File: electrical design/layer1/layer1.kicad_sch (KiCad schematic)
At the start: 226 parts, among them J1 XT30-F, J10 Conn_01x02_Pin, J11 Conn_01x01_Socket, J12 Conn_01x01_Socket, J13 SH1.0 5P, J14 SH1.0 3P, J15 Conn_01x01_Socket, J2 Conn_01x01_Socket, J3 Conn_01x01_Socket, J4 XT30PW-F, J5 Conn_01x01_Socket, J6 Conn_01x01_Socket, J7 Conn_01x01_Socket, J8 Conn_01x01_Socket, J9 Conn_01x02_Pin, Q1 MOSFET-NCH-FQP30N06L, Q2 MOSFET-NCH-AO3404A, SW1 SW_SPDT, U1 CD74HC4067SM, U2 CD74HC4067SM, U3 MOUDLE-SEEEDUINO-XIAO-ESP32C3

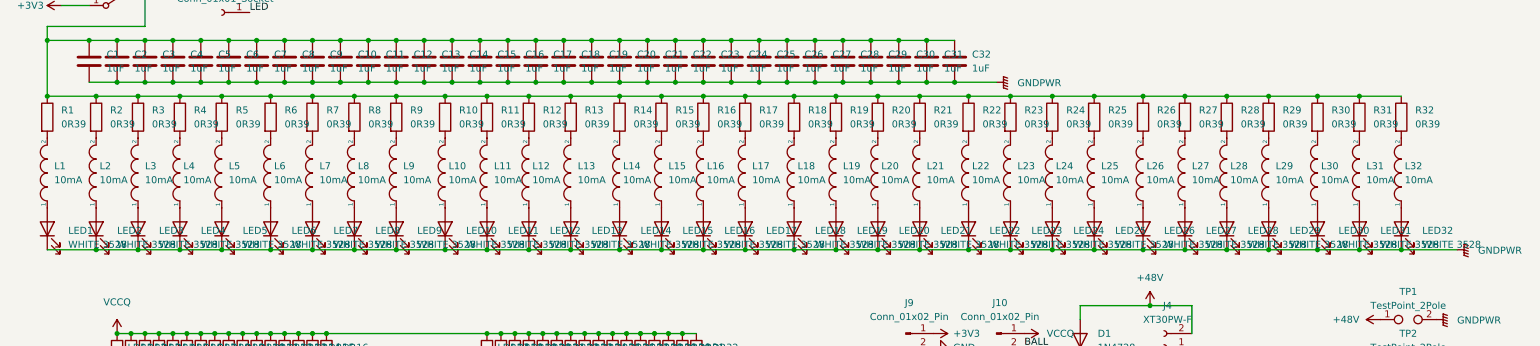
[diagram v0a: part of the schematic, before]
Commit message: correct led inductor value
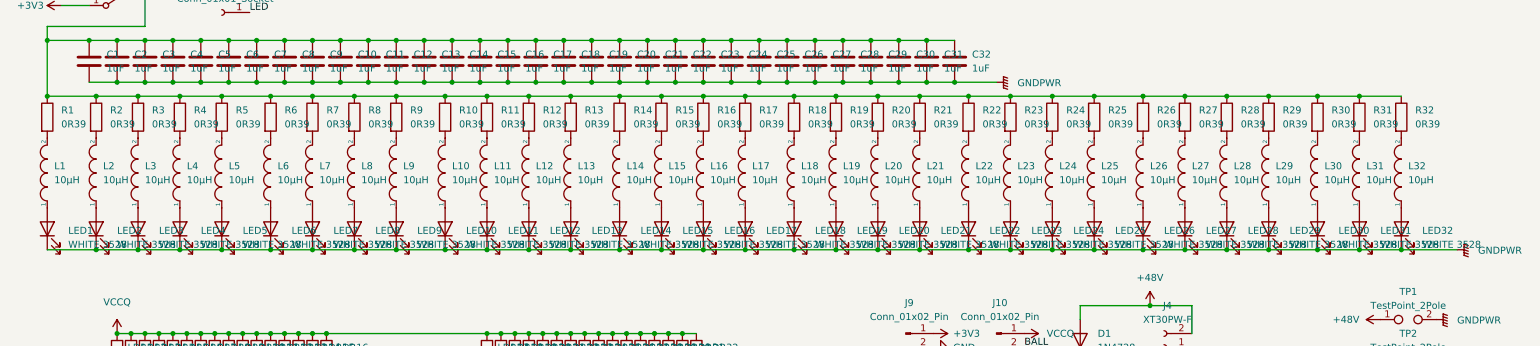
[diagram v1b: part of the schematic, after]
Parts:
- L1, L10, L11, L12, L13, L14, L15, L16, L17, L18, L19, L2, L20, L21, L22, L23, L24, L25, L26, L27, L28, L29, L3, L30, L31, L32, L4, L5, L6, L7, L8, L9: value 10mA -> 10µH

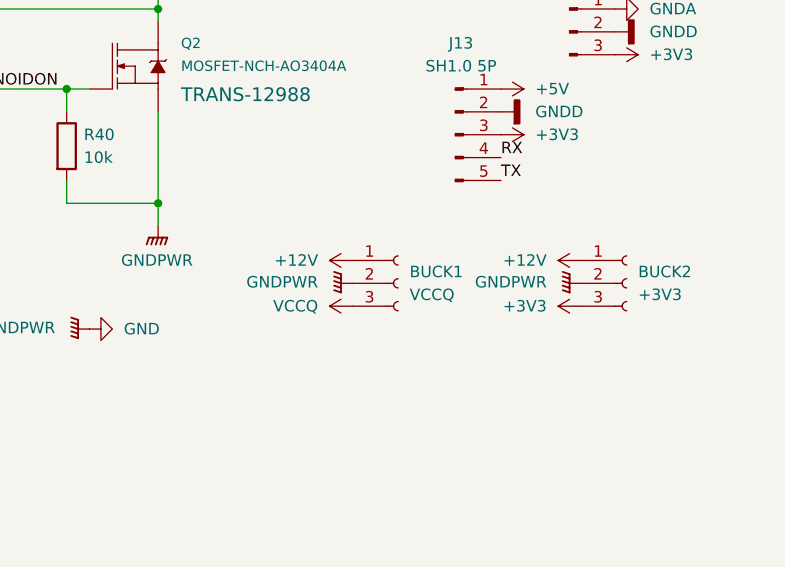
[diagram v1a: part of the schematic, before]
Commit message: correct reversed buck layout on l1 pcb
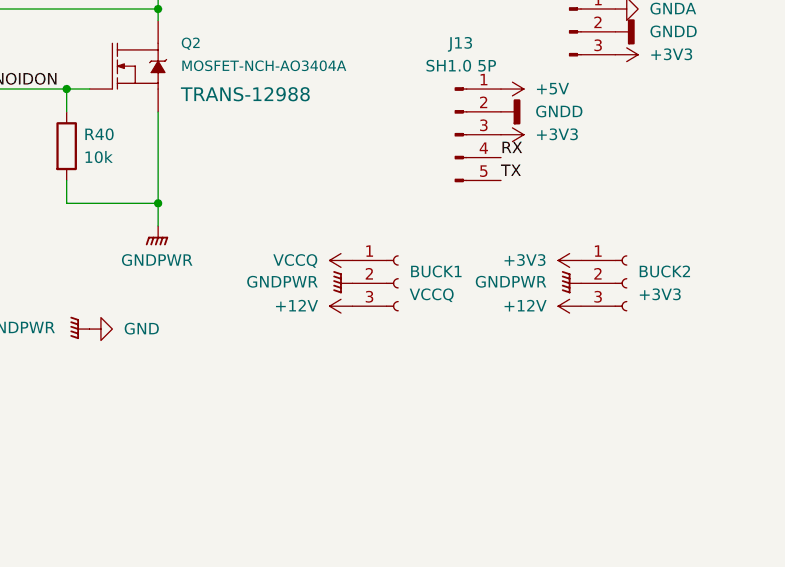
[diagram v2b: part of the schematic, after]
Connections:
- net +12V: now also BUCK1.3 (Pin_3), BUCK2.3 (Pin_3); no longer BUCK1.1 (Pin_1), BUCK2.1 (Pin_1)
- net +3V3: now also BUCK2.1 (Pin_1); no longer BUCK2.3 (Pin_3)
- net VCCQ: now also BUCK1.1 (Pin_1); no longer BUCK1.3 (Pin_3)
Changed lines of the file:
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@@
   (title_block
     (title "layer 1 schematic drawing")
-    (date "2023-11-10")
+    (date "2024-01-02")
+    (rev "1.1")
     (company "8076ducc Robotics Competition Team")
   )
@@
     )
   )
-  (symbol (lib_name "VCCQ_2") (lib_id "power:VCCQ") (at 245.11 156.21 90) (unit 1)
+  (symbol (lib_name "VCCQ_2") (lib_id "power:VCCQ") (at 245.11 151.13 90) (unit 1)
     (in_bom yes) (on_board yes) (dnp no) (fields_autoplaced)
-    (property "Reference" "#PWR019" (at 248.92 156.21 0)
+    (property "Reference" "#PWR019" (at 248.92 151.13 0)
       (effects (font (size 1.27 1.27)) hide)
     )
-    (property "Value" "VCCQ" (at 241.3 156.21 90)
+    (property "Value" "VCCQ" (at 241.3 151.13 90)
       (effects (font (size 1.27 1.27)) (justify left))
     )
-    (property "Footprint" "" (at 245.11 156.21 0)
+    (property "Footprint" "" (at 245.11 151.13 0)
       (effects (font (size 1.27 1.27)) hide)
     )
-    (property "Datasheet" "" (at 245.11 156.21 0)
+    (property "Datasheet" "" (at 245.11 151.13 0)
       (effects (font (size 1.27 1.27)) hide)
     )
@@
     )
   )
-  (symbol (lib_name "+12V_2") (lib_id "power:+12V") (at 270.51 151.13 90) (unit 1)
+  (symbol (lib_name "+12V_2") (lib_id "power:+12V") (at 270.51 156.21 90) (unit 1)
     (in_bom yes) (on_board yes) (dnp no) (fields_autoplaced)
-    (property "Reference" "#PWR024" (at 274.32 151.13 0)
+    (property "Reference" "#PWR024" (at 274.32 156.21 0)
       (effects (font (size 1.27 1.27)) hide)
     )
-    (property "Value" "+12V" (at 266.7 151.13 90)
+    (property "Value" "+12V" (at 266.7 156.21 90)
       (effects (font (size 1.27 1.27)) (justify left))
     )
-    (property "Footprint" "" (at 270.51 151.13 0)
+    (property "Footprint" "" (at 270.51 156.21 0)
       (effects (font (size 1.27 1.27)) hide)
     )
-    (property "Datasheet" "" (at 270.51 151.13 0)
+    (property "Datasheet" "" (at 270.51 156.21 0)
       (effects (font (size 1.27 1.27)) hide)
     )
@@
     )
   )
-  (symbol (lib_id "power:+3V3") (at 270.51 156.21 90) (unit 1)
-    (in_bom yes) (on_board yes) (dnp no) (fields_autoplaced)
-    (property "Reference" "#PWR021" (at 274.32 156.21 0)
-      (effects (font (size 1.27 1.27)) hide)
-    )
-    (property "Value" "+3V3" (at 266.7 156.2101 90)
-      (effects (font (size 1.27 1.27)) (justify left))
-    )
-    (property "Footprint" "" (at 270.51 156.21 0)
-      (effects (font (size 1.27 1.27)) hide)
-    )
-    (property "Datasheet" "" (at 270.51 156.21 0)
-      (effects (font (size 1.27 1.27)) hide)
-    )
-    (pin "1")
-    (instances
-      (project "layer1"
-        (path "/32d54464-fd6f-441d-9cef-d3e4fabf9fe1"
-          (reference "#PWR021") (unit 1)
-        )
-      )
-      (project "layer3"
-        (path "/d3bc7e0f-ae6c-4cdf-9591-eb9484f67211"
-          (reference "#PWR0111") (unit 1)
-        )
-      )
-    )
-  )
   (symbol (lib_id "pspice:INDUCTOR") (at 212.09 59.69 90) (unit 1)
     (in_bom yes) (on_board yes) (dnp no) (fields_autoplaced)
@@
     )
   )
+  (symbol (lib_id "power:+3V3") (at 270.51 151.13 90) (unit 1)
+    (in_bom yes) (on_board yes) (dnp no) (fields_autoplaced)
+    (property "Reference" "#PWR021" (at 274.32 151.13 0)
+      (effects (font (size 1.27 1.27)) hide)
+    )
+    (property "Value" "+3V3" (at 266.7 151.1301 90)
+      (effects (font (size 1.27 1.27)) (justify left))
+    )
+    (property "Footprint" "" (at 270.51 151.13 0)
+      (effects (font (size 1.27 1.27)) hide)
+    )
+    (property "Datasheet" "" (at 270.51 151.13 0)
+      (effects (font (size 1.27 1.27)) hide)
+    )
+    (pin "1")
+    (instances
+      (project "layer1"
+        (path "/32d54464-fd6f-441d-9cef-d3e4fabf9fe1"
+          (reference "#PWR021") (unit 1)
+        )
+      )
+      (project "layer3"
+        (path "/d3bc7e0f-ae6c-4cdf-9591-eb9484f67211"
+          (reference "#PWR0111") (unit 1)
+        )
+      )
+    )
+  )
   (symbol (lib_id "Device:LED") (at 140.97 69.85 90) (unit 1)
     (in_bom yes) (on_board yes) (dnp no) (fields_autoplaced)
@@
     )
   )
+  (symbol (lib_name "+12V_2") (lib_id "power:+12V") (at 245.11 156.21 90) (unit 1)
+    (in_bom yes) (on_board yes) (dnp no) (fields_autoplaced)
+    (property "Reference" "#PWR023" (at 248.92 156.21 0)
+      (effects (font (size 1.27 1.27)) hide)
+    )
+    (property "Value" "+12V" (at 241.3 156.21 90)
+      (effects (font (size 1.27 1.27)) (justify left))
+    )
+    (property "Footprint" "" (at 245.11 156.21 0)
+      (effects (font (size 1.27 1.27)) hide)
+    )
+    (property "Datasheet" "" (at 245.11 156.21 0)
+      (effects (font (size 1.27 1.27)) hide)
+    )
+    (pin "1")
+    (instances
+      (project "layer1"
+        (path "/32d54464-fd6f-441d-9cef-d3e4fabf9fe1"
+          (reference "#PWR023") (unit 1)
+        )
+      )
+    )
+  )
   (symbol (lib_id "Device:R") (at 62.23 49.53 0) (unit 1)
     (in_bom yes) (on_board yes) (dnp no) (fields_autoplaced)
@@
         )
       )
-    )
-  )
-  (symbol (lib_name "+12V_2") (lib_id "power:+12V") (at 245.11 151.13 90) (unit 1)
-    (in_bom yes) (on_board yes) (dnp no) (fields_autoplaced)
-    (property "Reference" "#PWR023" (at 248.92 151.13 0)
-      (effects (font (size 1.27 1.27)) hide)
-    )
-    (property "Value" "+12V" (at 241.3 151.13 90)
-      (effects (font (size 1.27 1.27)) (justify left))
-    )
-    (property "Footprint" "" (at 245.11 151.13 0)
-      (effects (font (size 1.27 1.27)) hide)
-    )
-    (property "Datasheet" "" (at 245.11 151.13 0)
-      (effects (font (size 1.27 1.27)) hide)
-    )
-    (pin "1")
-    (instances
-      (project "layer1"
-        (path "/32d54464-fd6f-441d-9cef-d3e4fabf9fe1"
-          (reference "#PWR023") (unit 1)
-        )
-      )
